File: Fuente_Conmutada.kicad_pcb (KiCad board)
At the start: 2 copper layers, 48 parts, among them J1 Terminal_220v, J2 Terminal_12v, J3 Vout, Q1 IRF840, Q2 IRF840, T1 Transformer_1P_SS, U1 TL494, U2 IR2110

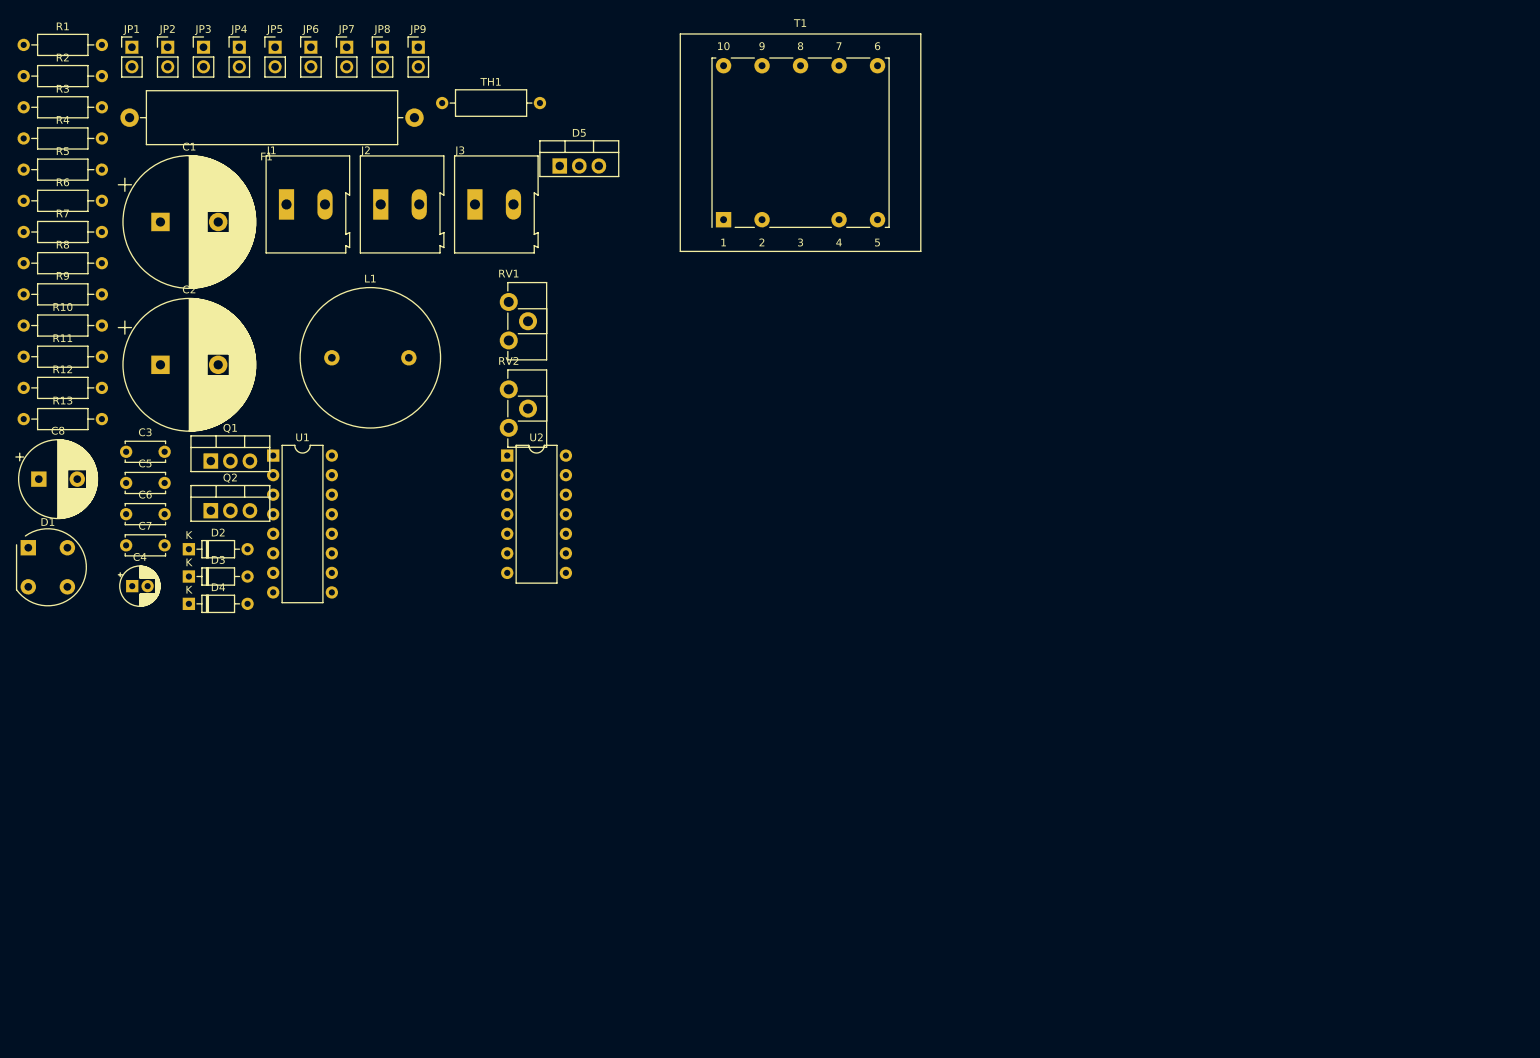
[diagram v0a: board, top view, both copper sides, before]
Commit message: Footprints correctos agregados
- Hice y puse el footprint del transformador
- Corregí algunos otros footprints como el del puente de diodos por el que tenemos realmente y el portafusible
- Actualicé los componentes eso en el editor de PCB y puse un cuadrado de 10x10cm donde se hace el PCB
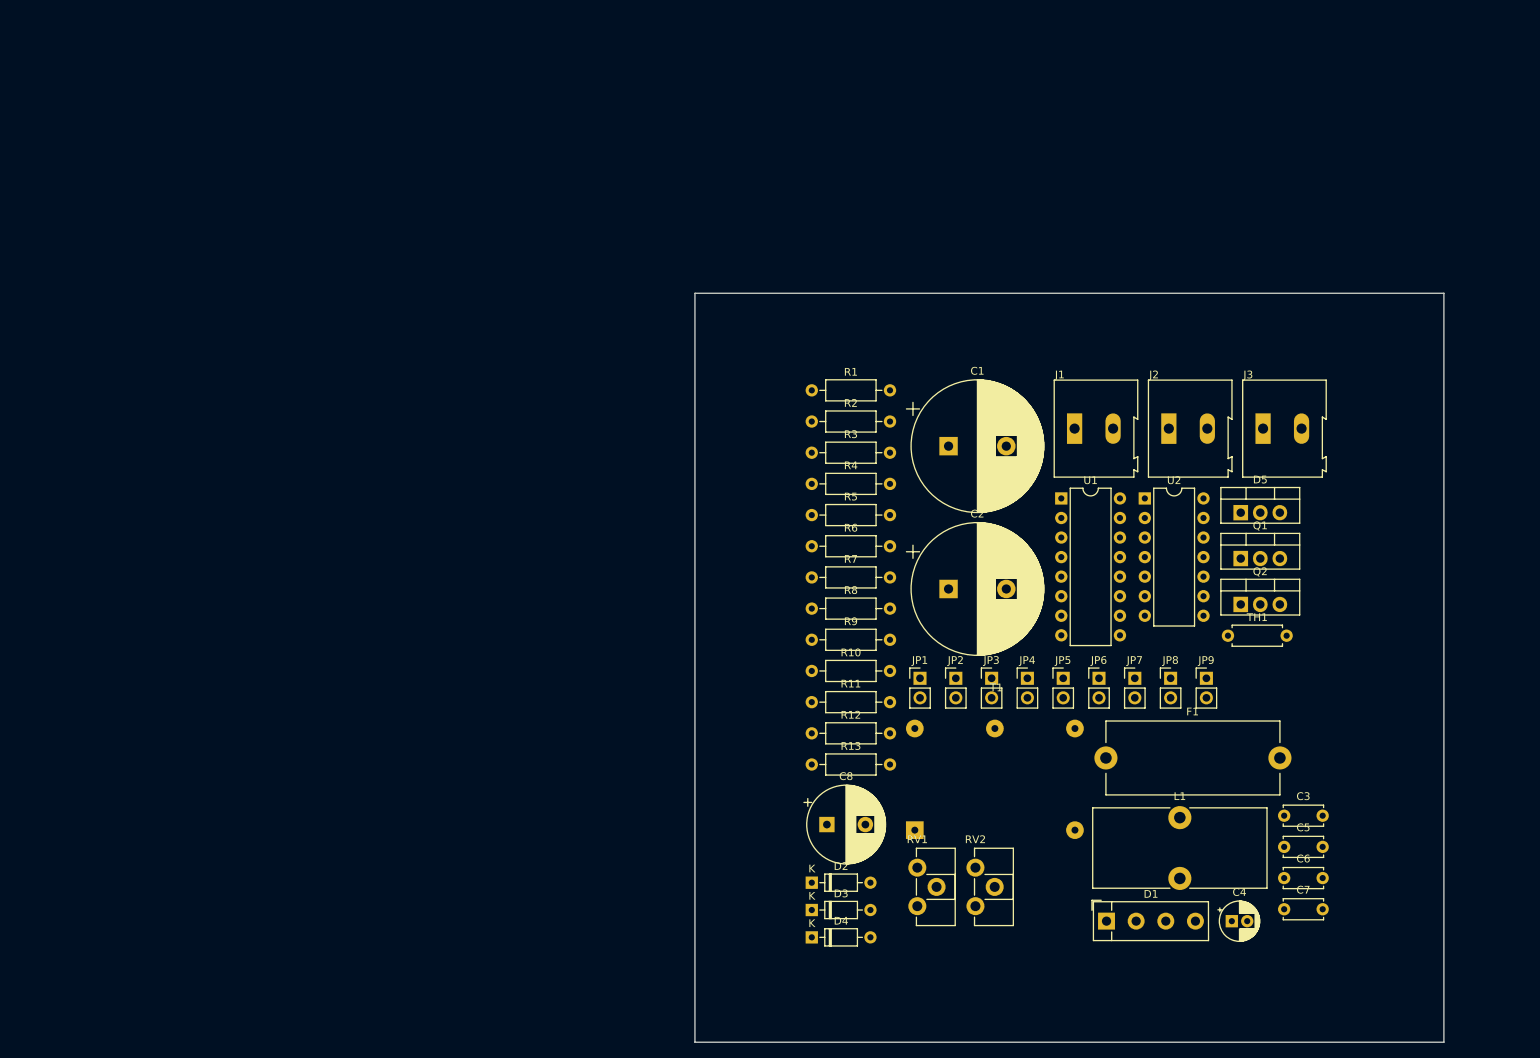
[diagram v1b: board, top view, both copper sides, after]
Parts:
- D1: footprint Diode_THT:Diode_Bridge_Round_D9.8mm -> Diode_THT:Diode_Bridge_Vishay_KBPM
- F1: footprint Fuse:Fuse_SunFuse-6HP -> Fuse:Fuseholder_Cylinder-5x20mm_Stelvio-Kontek_PTF78_Horizontal_Open
- L1: footprint Inductor_THT:L_Radial_D18.0mm_P10.00mm -> Inductor_THT:L_Toroid_Vertical_L22.4mm_W10.2mm_P7.90mm_Vishay_TJ4
- T1: footprint Transformer_THT:Transformer_Breve_TEZ-28x33 -> TransformerLib:Ferrite_Core_Trans
- TH1: footprint Resistor_THT:R_Axial_DIN0309_L9.0mm_D3.2mm_P12.70mm_Horizontal -> Resistor_THT:R_Axial_DIN0207_L6.3mm_D2.5mm_P7.62mm_Horizontal
- moved C3 157.7 mm to (182.2, 117.9)
- moved C6 157.7 mm to (182.2, 126.0)
- moved C7 157.7 mm to (182.2, 130.0)
- moved C5 157.7 mm to (182.2, 121.9)
- moved F1 151.7 mm to (159.0, 110.4)
- moved C4 149.3 mm to (175.4, 131.6)
- moved D1 148.2 mm to (159.1, 131.6)
- moved Q1 134.4 mm to (176.6, 84.5)
- moved Q2 134.3 mm to (176.6, 90.5)
- moved JP1 131.1 mm to (134.9, 100.0)
- moved JP2 131.1 mm to (139.5, 100.0)
- moved JP3 131.1 mm to (144.2, 100.0)
- moved JP4 131.1 mm to (148.8, 100.0)
- moved JP5 131.1 mm to (153.5, 100.0)
- moved JP6 131.1 mm to (158.1, 100.0)
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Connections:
- R1 pad 2: Net-(R1-Pad2) -> Net-(JP2-A)
- R2 pad 1: Net-(R1-Pad2) -> Net-(JP2-A)
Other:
- board outline added: 97.3 x 97.3 mm

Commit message: eq
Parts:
- removed JP9: Jumper, Connector_PinHeader_2.54mm:PinHeader_1x02_P2.54mm_Vertical
- L1: moved to B.Cu
- moved J2 91.0 mm to (86.6, 109.8), turned to 90 degrees
- moved R13 86.5 mm to (194.9, 66.5), turned to 180 degrees
- moved C8 80.2 mm to (202.7, 112.3), turned to 90 degrees
- moved D1 78.4 mm to (101.9, 78.1), turned to -90 degrees
- moved D3 76.0 mm to (175.9, 77.7), turned to 180 degrees
- moved F1 72.4 mm to (104.4, 62.9), turned to 180 degrees
- moved J1 70.7 mm to (86.6, 85.6), turned to 90 degrees
- moved D4 66.4 mm to (156.6, 77.7), turned to 180 degrees
- moved C6 66.2 mm to (198.9, 62.0), turned to 180 degrees
- moved C7 66.1 mm to (199.0, 66.2), turned to -90 degrees
- moved TH1 65.9 mm to (117.1, 62.9), turned to 180 degrees
- moved R12 65.4 mm to (177.2, 73.9), turned to 180 degrees
- moved U1 63.6 mm to (100.6, 112.4), turned to 90 degrees
- moved C5 63.1 mm to (123.3, 99.2)
- moved R9 62.1 mm to (177.2, 68.8), turned to 180 degrees
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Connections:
- net 1 renamed GND
- net Net-(J1-Pin_2) renamed VAC
- C4 pad 2: Net-(U2-VS) -> Vs
- C5 pad 2: Net-(U2-VS) -> Vs
- D3 pad 1: Net-(D3-K) -> HO
- D4 pad 1: Net-(D4-K) -> LO
- JP2 pad 2: Net-(JP2-B) -> /Punto_medio
- JP3 pad 2: unconnected-(JP3-B-Pad2) -> PWM1
- JP4 pad 2: unconnected-(JP4-B-Pad2) -> PWM2
- JP5 pad 2: unconnected-(JP5-B-Pad2) -> HO
- JP6 pad 2: unconnected-(JP6-B-Pad2) -> LO
- JP7 pad 1: Net-(JP2-B) -> Vs
- Q1 pad 3: Net-(JP2-B) -> Vs
- Q2 pad 2: Net-(JP2-B) -> Vs
- R10 pad 1: Net-(D4-K) -> LO
- R12 pad 1: Net-(D3-A) -> Vs
- R12 pad 2: Net-(JP2-B) -> Net-(D3-A)
- R13 pad 2: Net-(JP2-B) -> /Punto_medio
- R3 pad 1: Net-(U1-1IN-) -> Vref
- R5 pad 1: Net-(U1-1IN-) -> Vref
- R9 pad 1: Net-(D3-K) -> HO
- T1 pad 2: Net-(JP2-B) -> /Punto_medio
- T1 pad 3: Net-(JP9-A) -> Net-(D5-A2)
- U1 pad 13: unconnected-(U1-OUTCTRL-Pad13) -> Vref
- U1 pad 14: unconnected-(U1-REF-Pad14) -> Vref
- U1 pad 15: Net-(U1-1IN-) -> Vref
- U1 pad 2: Net-(U1-1IN-) -> Vref
- U2 pad 10: unconnected-(U2-HIN-Pad10) -> PWM1
- U2 pad 12: unconnected-(U2-LIN-Pad12) -> PWM2
- U2 pad 5: Net-(U2-VS) -> Vs
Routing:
- net GND: track 0.00 -> 388.6 mm, vias 0 -> 6
- net Vs: track 0.00 -> 140.7 mm, vias 0 -> 4
- net +12V: track 0.00 -> 112.6 mm
- net /Punto_medio: track 0.00 -> 65.7 mm, vias 0 -> 2
- net Net-(JP2-A): track 0.00 -> 56.5 mm
- net Net-(JP4-A): track 0.00 -> 53.3 mm
- net Net-(D1-+): track 0.00 -> 51.9 mm
- net HO: track 0.00 -> 51.9 mm
- net Net-(JP3-A): track 0.00 -> 50.8 mm
- net Net-(J3-Pin_1): track 0.00 -> 47.1 mm
- net Net-(JP1-B): track 0.00 -> 44.8 mm
- net 2: track 0.00 -> 44.7 mm
- net Net-(T1-AA): track 0.00 -> 43.5 mm
- net Vref: track 0.00 -> 41.4 mm
- net PWM1: track 0.00 -> 41.2 mm
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- added copper zone on B.Cu, net GND
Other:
- board size 97.3 x 97.3 mm -> 135 x 85 mm
- board text added: "150k"
- board text added: "R1"
- board text added: "R2"

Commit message: dawd
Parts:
- moved R4 3.03 mm to (120.1, 127.3)
- moved R8 3.03 mm to (140.4, 127.3)
- moved RV1 3.03 mm to (107.4, 127.3)
- moved C4 3.03 mm to (131.5, 97.0)
- moved C1 3.03 mm to (131.5, 85.2)
- moved C2 3.03 mm to (131.5, 64.9)
- moved C3 3.03 mm to (127.7, 117.7)
- moved C5 3.03 mm to (122.5, 96.3)
- moved C6 3.03 mm to (198.1, 59.1)
- moved C7 3.03 mm to (198.2, 63.3)
- moved C8 3.03 mm to (201.8, 109.4)
- moved D1 3.03 mm to (101.0, 75.2)
- moved D2 3.03 mm to (124.5, 99.3)
- moved D3 3.03 mm to (175.0, 74.8)
- moved D5 3.03 mm to (176.6, 123.7)
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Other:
- board text added: "${REFERENCE}"

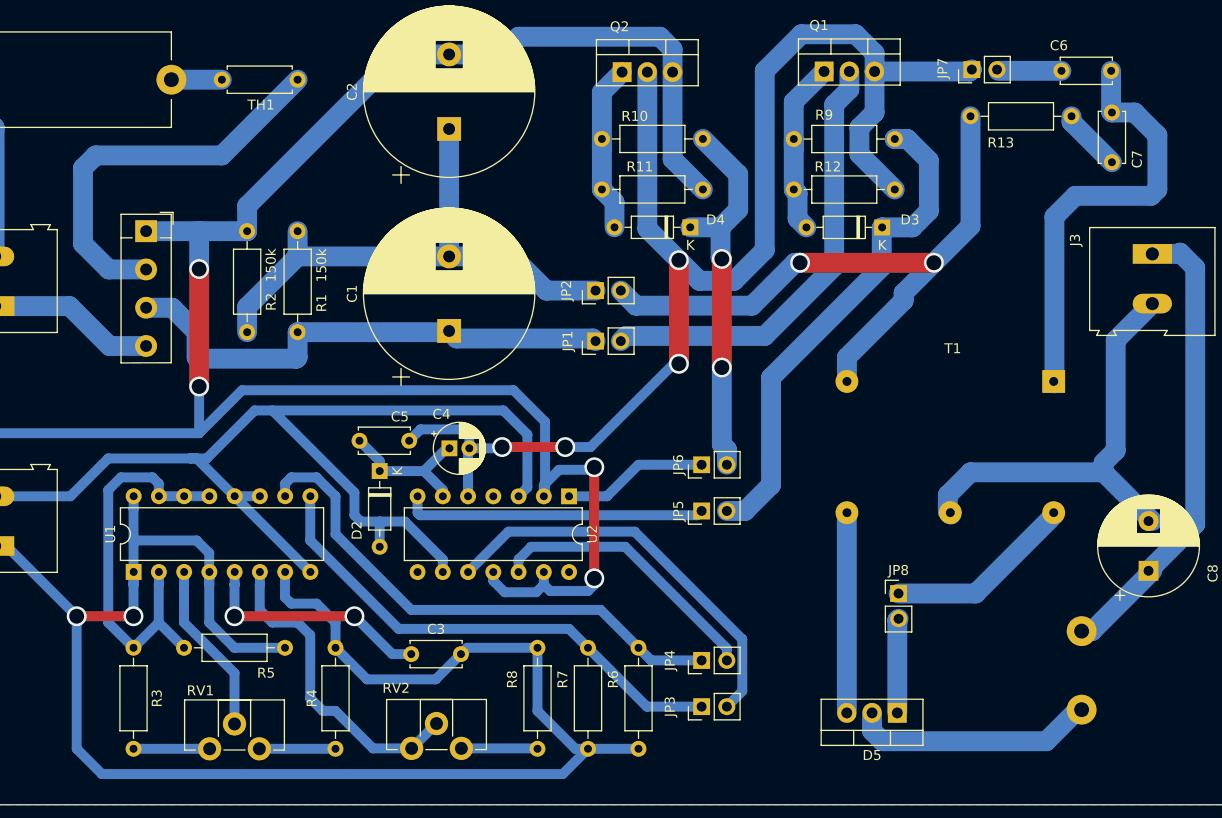
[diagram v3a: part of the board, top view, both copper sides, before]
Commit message: Pinout de puente, tamaño de pads y no mucho mas
-Cambié el pinout del puente por el que tenemos realmente
-Cambié el tamaño de todos los pads a mínimo 2mm
-Retoque en alguna que otra pista, casi nada

Ahora hay varios warnings, que son porque el silkscreen choca con algo, pero no pasa nada crítico con eso
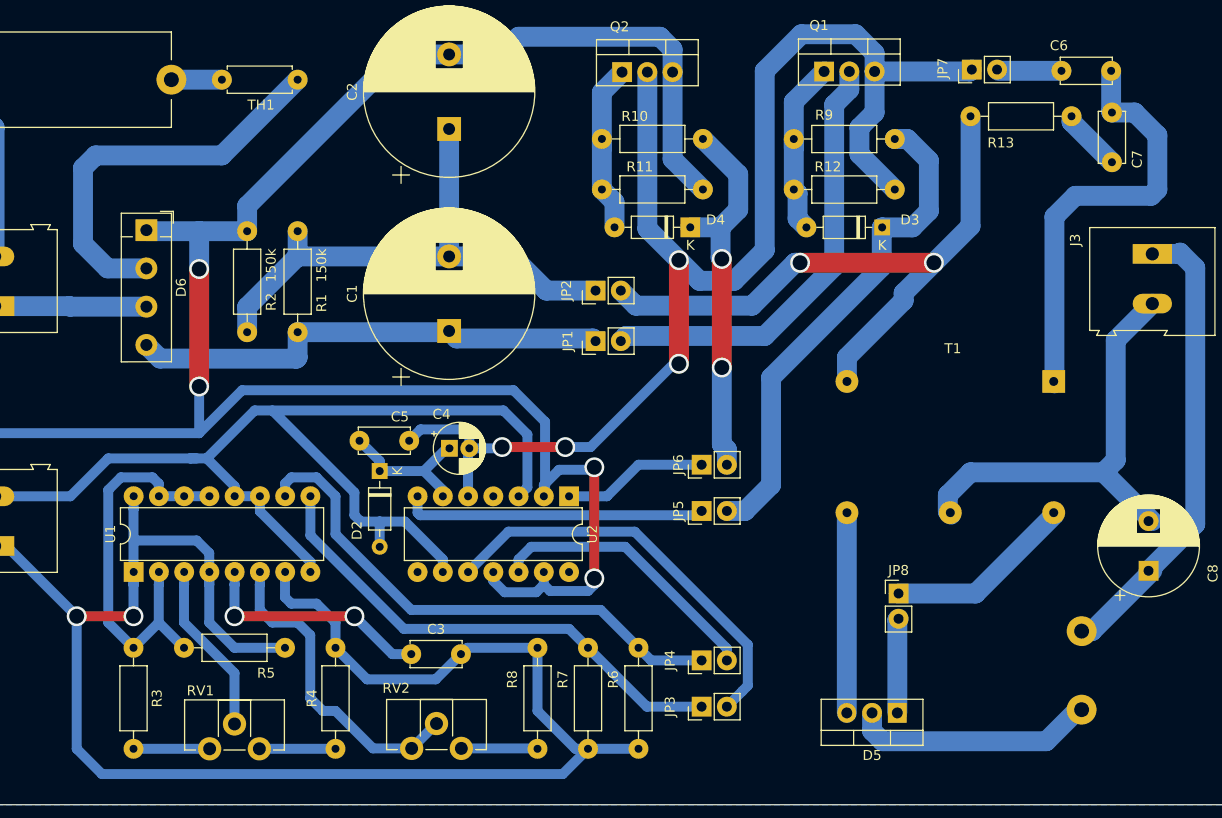
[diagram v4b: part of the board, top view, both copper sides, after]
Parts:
- removed D1: B80C2300-1500B, Diode_THT:Diode_Bridge_Vishay_KBPM
- added D6: B40C2300-1500A, Diode_THT:Diode_Bridge_Vishay_KBPM, F.Cu at (101.0, 75.1)
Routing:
- net Net-(D6-+): track 51.9 -> 48.8 mm
- net GND_AC: track 16.9 -> 15.3 mm
- net +12V: track 112.6 -> 111.1 mm
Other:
- board text removed: "${REFERENCE}"
